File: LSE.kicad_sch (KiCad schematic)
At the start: 5 parts, among them Y1 32.758kHz

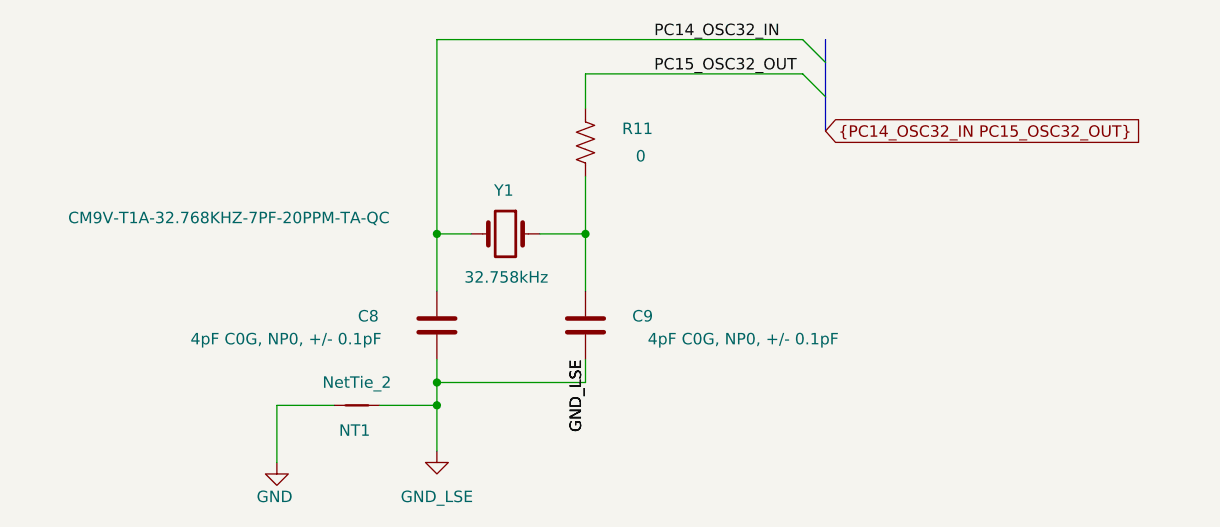
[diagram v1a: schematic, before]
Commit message: added footprint and step model. Cleaned up silkscreen and fab layers.
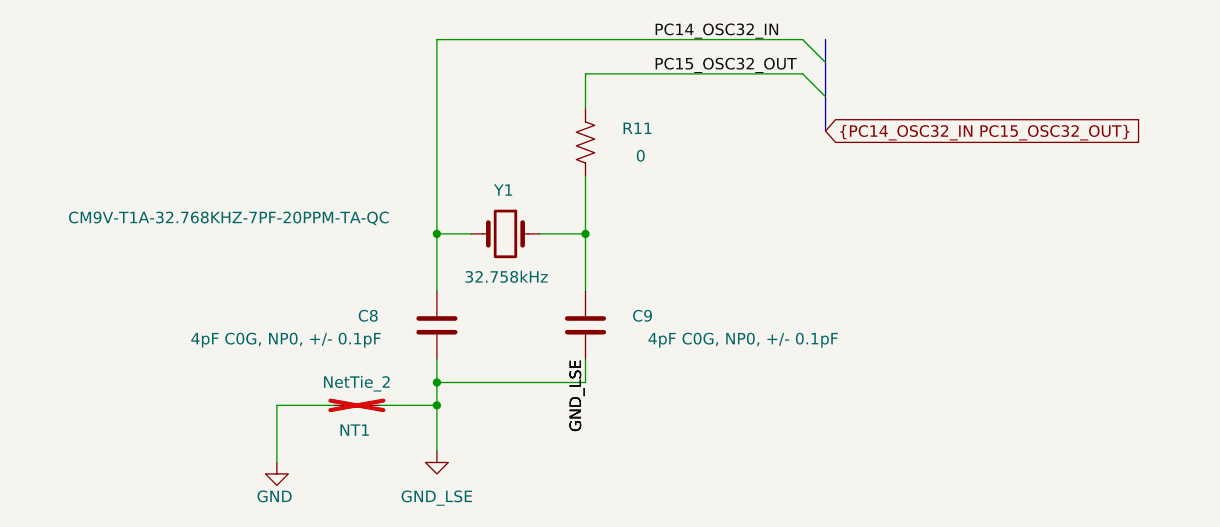
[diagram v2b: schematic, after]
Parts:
- NT1: now not fitted
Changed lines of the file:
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@@
 		(in_bom no)
 		(on_board yes)
-		(dnp no)
+		(dnp yes)
 		(property "Reference" "NT1"
 			(at 103.886 117.094 0)
